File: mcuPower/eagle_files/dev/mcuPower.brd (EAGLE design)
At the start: 27 x 45 mm, 8 parts, among them P1 CR2032, P2 CR2032, U1 PQ070XF01SZH

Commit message: various changes + production files. Reroutes, library footprint changes, and moving pot to front side of board
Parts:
- moved R2 3.31 mm to (20.4, 4.19), flipped to the top
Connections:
- net VOUT: now also R2.E; no longer R2.A
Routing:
- net VOUT: track 41.1 -> 44.2 mm, vias 1 -> 0
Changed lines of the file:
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@@
 <attribute name="VALUE" x="12.319" y="9.774" size="1.27" layer="28" rot="MR0"/>
 </element>
-<element name="R2" library="pot" package="B25P" value="" x="17.11" y="4.49" smashed="yes" rot="MR0">
-<attribute name="NAME" x="23.585" y="3.5" size="1.27" layer="26" ratio="10" rot="MR0"/>
-<attribute name="VALUE" x="20.2596" y="-0.59" size="1.27" layer="28" ratio="10" rot="MR0"/>
+<element name="R2" library="pot" package="B25P" value="" x="20.41" y="4.19" smashed="yes">
+<attribute name="NAME" x="13.935" y="3.2" size="1.27" layer="25" ratio="10"/>
+<attribute name="VALUE" x="17.2604" y="-0.89" size="1.27" layer="27" ratio="10"/>
 </element>
 <element name="JP1" library="SparkFun-Connectors" package="1X04" value="" x="2.02" y="2.02" smashed="yes">
@@
 <signal name="N$2">
 <contactref element="R1" pad="1"/>
-<contactref element="R2" pad="S"/>
 <contactref element="U1" pad="VADJ"/>
 <wire x1="22.4" y1="18.01" x2="13.57" y2="18.01" width="0.4064" layer="16"/>
 <wire x1="13.57" y1="18.01" x2="12.5" y2="16.94" width="0.4064" layer="16"/>
-<wire x1="17.11" y1="7.03" x2="17.11" y2="7.21" width="0.4064" layer="1"/>
-<wire x1="17.11" y1="7.21" x2="19.3" y2="9.4" width="0.4064" layer="1"/>
-<wire x1="19.3" y1="9.4" x2="19.3" y2="14.91" width="0.4064" layer="1"/>
-<wire x1="19.3" y1="14.91" x2="22.4" y2="18.01" width="0.4064" layer="1"/>
+<contactref element="R2" pad="S"/>
+<wire x1="22.4" y1="18.01" x2="21.61" y2="18.01" width="0.4064" layer="1"/>
+<wire x1="21.61" y1="18.01" x2="19.4" y2="15.8" width="0.4064" layer="1"/>
+<wire x1="19.4" y1="15.8" x2="19.4" y2="7.74" width="0.4064" layer="1"/>
+<wire x1="19.4" y1="7.74" x2="20.41" y2="6.73" width="0.4064" layer="1"/>
 </signal>
 <signal name="VOUT">
 <contactref element="C2" pad="1"/>
 <contactref element="JP1" pad="2"/>
-<contactref element="R2" pad="A"/>
 <contactref element="U1" pad="VOUT"/>
 <wire x1="22.4" y1="12.93" x2="13.15" y2="12.93" width="0.4064" layer="16"/>
 <wire x1="13.15" y1="12.93" x2="12.28" y2="12.06" width="0.4064" layer="16"/>
-<wire x1="19.65" y1="4.49" x2="19.69" y2="4.49" width="0.4064" layer="1"/>
-<wire x1="19.69" y1="4.49" x2="25.1" y2="9.9" width="0.4064" layer="1"/>
-<via x="25.1" y="9.9" extent="1-16" drill="0.6"/>
-<wire x1="25.1" y1="9.9" x2="25.1" y2="11.4" width="0.4064" layer="16"/>
-<wire x1="25.1" y1="11.4" x2="23.6" y2="12.9" width="0.4064" layer="16"/>
-<wire x1="23.6" y1="12.9" x2="22.43" y2="12.9" width="0.4064" layer="16"/>
-<wire x1="22.43" y1="12.9" x2="22.4" y2="12.93" width="0.4064" layer="16"/>
+<contactref element="R2" pad="E"/>
+<wire x1="22.4" y1="12.93" x2="23.57" y2="12.93" width="0.4064" layer="16"/>
+<wire x1="23.57" y1="12.93" x2="25.3" y2="11.2" width="0.4064" layer="16"/>
+<wire x1="25.3" y1="11.2" x2="25.3" y2="6.54" width="0.4064" layer="16"/>
+<wire x1="25.3" y1="6.54" x2="22.95" y2="4.19" width="0.4064" layer="16"/>
 <wire x1="4.56" y1="2.02" x2="4.56" y2="2.06" width="0.4064" layer="1"/>
-<wire x1="4.56" y1="2.06" x2="7.1" y2="4.6" width="0.4064" layer="1"/>
-<wire x1="7.1" y1="4.6" x2="11.1" y2="4.6" width="0.4064" layer="1"/>
-<wire x1="11.1" y1="4.6" x2="13.5" y2="2.2" width="0.4064" layer="1"/>
-<wire x1="13.5" y1="2.2" x2="17.36" y2="2.2" width="0.4064" layer="1"/>
-<wire x1="17.36" y1="2.2" x2="19.65" y2="4.49" width="0.4064" layer="1"/>
+<wire x1="4.56" y1="2.06" x2="7.2" y2="4.7" width="0.4064" layer="1"/>
+<wire x1="7.2" y1="4.7" x2="10.3" y2="4.7" width="0.4064" layer="1"/>
+<wire x1="10.3" y1="4.7" x2="13.7" y2="1.3" width="0.4064" layer="1"/>
+<wire x1="13.7" y1="1.3" x2="20.06" y2="1.3" width="0.4064" layer="1"/>
+<wire x1="20.06" y1="1.3" x2="22.95" y2="4.19" width="0.4064" layer="1"/>
 </signal>
 <signal name="KEY">

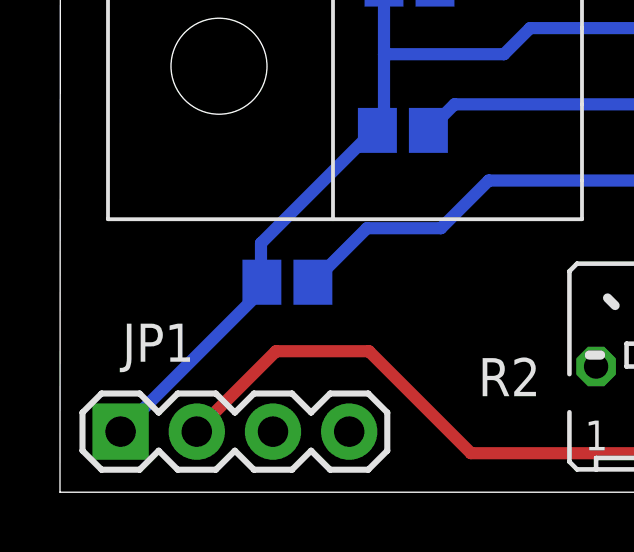
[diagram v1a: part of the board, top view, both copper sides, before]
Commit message: added extra header pin to stabilize board
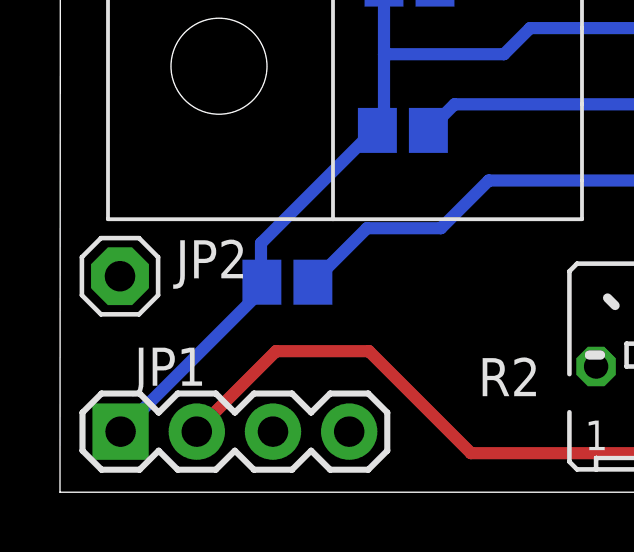
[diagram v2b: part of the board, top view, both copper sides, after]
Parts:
- added JP2: (no value), adafruit:1X01
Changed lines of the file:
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@@
 </element>
 <element name="JP1" library="SparkFun-Connectors" package="1X04" value="" x="2.02" y="2.02" smashed="yes">
-<attribute name="NAME" x="2.0738" y="4.3488" size="1.27" layer="25" ratio="10"/>
+<attribute name="NAME" x="2.4738" y="3.5488" size="1.27" layer="25" ratio="10"/>
 <attribute name="VALUE" x="0.75" y="-1.155" size="1.27" layer="27"/>
 </element>
@@
 <attribute name="NAME" x="21.29" y="39.84" size="1.27" layer="26" rot="MR180"/>
 </element>
+<element name="JP2" library="adafruit" package="1X01" value="" x="2" y="7.2" smashed="yes">
+<attribute name="NAME" x="3.8538" y="7.1288" size="1.27" layer="25" ratio="10"/>
+<attribute name="VALUE" x="0.73" y="4.025" size="1.27" layer="27"/>
+</element>
 </elements>
